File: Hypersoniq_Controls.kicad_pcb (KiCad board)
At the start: 2 copper layers, 40.4 x 110 mm, 15 parts, among them J1 Conn_01x10_Pin, J11 Freq_In, J12 Audio_Mix_4Pole, J2 Conn_01x10_Pin, J3 Conn_01x10_Pin, J4 Audio_In, J5 Audio_Out_1P, J6 Audio_Mix_1Pole, J7 Freq_CV, J8 Audio_Out_4P

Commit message: Started laying out Panel
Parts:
- moved J12 3.20 mm to (83.1, 141.5)
- moved J6 3.20 mm to (57.8, 141.5)
- moved J11 2.10 mm to (70.2, 140.0)
- moved TP4 0.43 mm to (86.9, 147.4)
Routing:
- net /AUDIO_MIX_4POLE: track 66.3 -> 69.5 mm
- net /AUDIO_MIX_1POLE: track 67.0 -> 70.1 mm
- net /FREQ_CV3: track 56.6 -> 58.7 mm
- net /AUDIO_IN3: track 55.1 -> 56.4 mm
- net /AUDIO_IN4: track 57.9 -> 58.9 mm
- net /FREQ_JACK: track 13.7 -> 12.7 mm

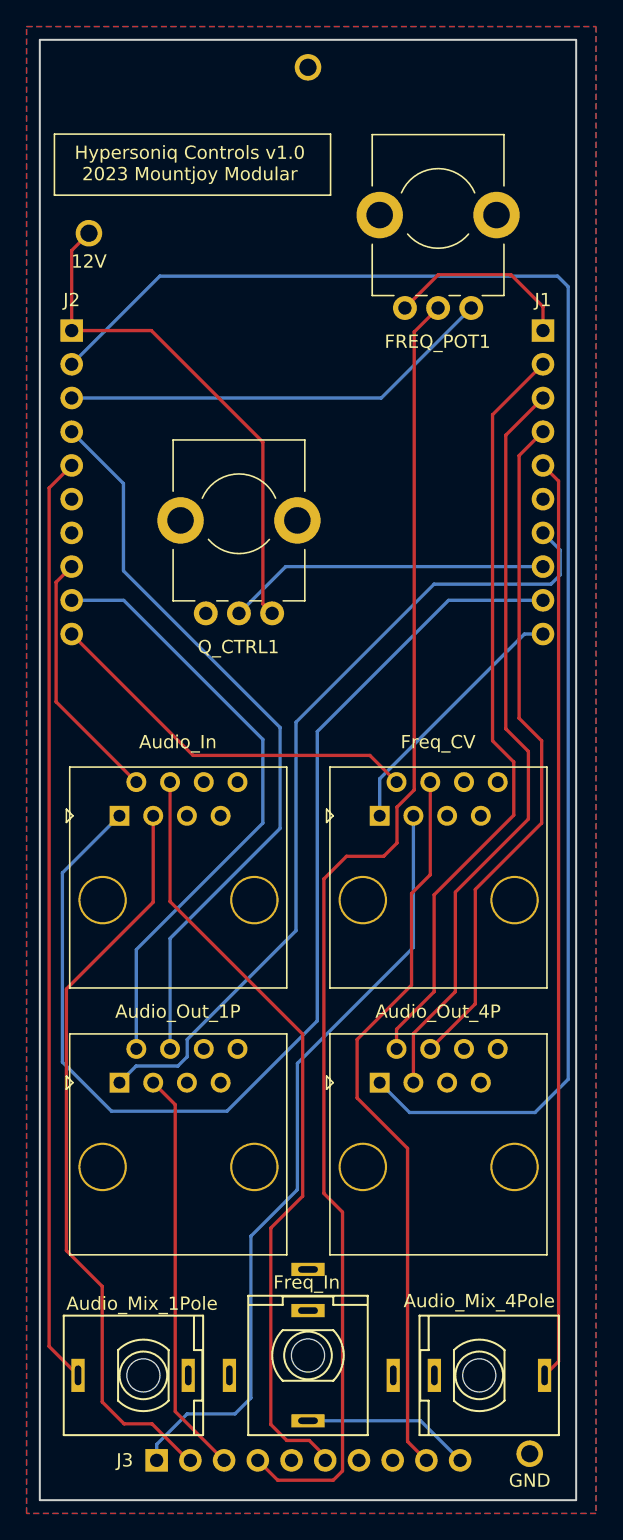
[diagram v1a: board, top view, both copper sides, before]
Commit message: Started generating JLC placement details
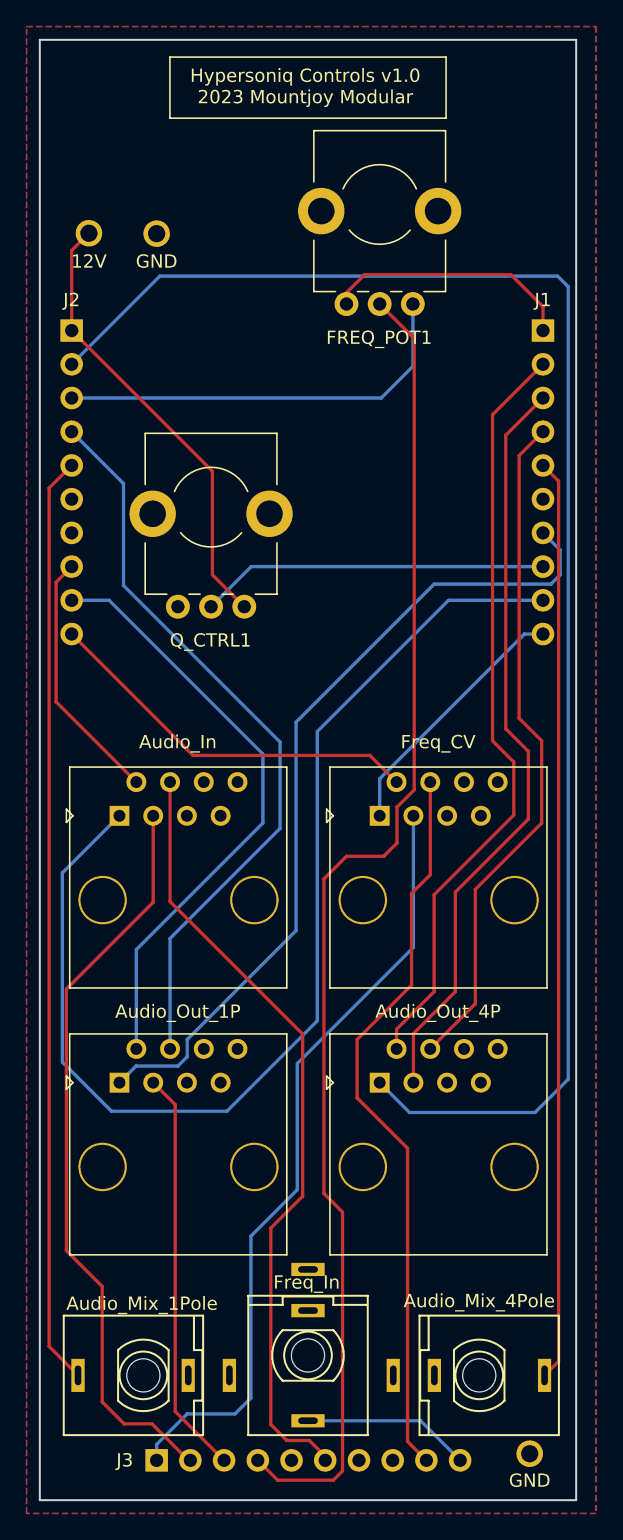
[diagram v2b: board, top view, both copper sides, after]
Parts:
- moved TP3 16.9 mm to (58.8, 55.5)
- moved FREQ_POT1 4.41 mm to (75.6, 53.3)
- moved Q_CTRL1 2.16 mm to (62.9, 76.1)
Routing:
- net +12V: track 38.9 -> 34.1 mm
- net /FREQ_POT_VL: track 14.2 -> 19.0 mm
- net /Q_POT: track 24.4 -> 26.3 mm
- net /FREQ_POT_VH: track 32.9 -> 31.4 mm
- net /1POLE_OUT2: track 46.0 -> 45.4 mm
- net /FREQ_POT: track 100.7 -> 101.3 mm
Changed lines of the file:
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@@
   (net 43 "unconnected-(J12-Pad2)")
   (footprint "Custom_Footprints:1.3mm_Test_Point" (layer "F.Cu")
-    (at 70.2 42.97)
+    (at 58.8 55.5)
     (descr "1.3mm Test Point")
     (tags "Through Hole Mount Test Points")
@@
   )
   (footprint "Custom_Footprints:Alpha_9mm_Potentiometer_Aligned" (layer "F.Cu")
-    (at 65 76.6)
+    (at 62.9 76.1)
     (descr "Potentiometer 9mm")
     (tags "Potentiometer 9mm")
@@
   )
   (footprint "Custom_Footprints:Alpha_9mm_Potentiometer_Aligned" (layer "F.Cu")
-    (at 80 53.6)
+    (at 75.6 53.3)
     (descr "Potentiometer 9mm")
     (tags "Potentiometer 9mm")
@@
     )
   )
-  (gr_rect (start 51.1 48) (end 71.9 52.6)
+  (gr_rect (start 59.8 42.2) (end 80.6 46.8)
     (stroke (width 0.12) (type default)) (fill none) (layer "F.SilkS"))
   (gr_rect (start 57 146.1) (end 83.45 149.7)
@@
   (gr_line (start 90.4 40.9) (end 90.4 150.9)
     (stroke (width 0.15) (type solid)) (layer "Edge.Cuts"))
-  (gr_text "GND" (at 70.2 45) (layer "B.SilkS")
-    (effects (font (size 1.2 1.2) (thickness 0.2)) (justify mirror))
+  (gr_text "GND" (at 58.8 57.53) (layer "B.SilkS")
+    (effects (font (size 1 1) (thickness 0.2)) (justify mirror))
   )
   (gr_text "GND" (at 87 149.43) (layer "B.SilkS")
@@
     (effects (font (size 1 1) (thickness 0.2)) (justify mirror))
   )
+  (gr_text "GND" (at 58.8 57.6) (layer "F.SilkS")
+    (effects (font (size 1 1) (thickness 0.2)))
+  )
   (gr_text "J3" (at 56.4 147.9) (layer "F.SilkS")
     (effects (font (size 1 1) (thickness 0.15)))
   )
-  (gr_text "Hypersoniq Controls v1.0\n2023 Mountjoy Modular" (at 61.3 51.6) (layer "F.SilkS")
+  (gr_text "Hypersoniq Controls v1.0\n2023 Mountjoy Modular" (at 70 45.8) (layer "F.SilkS")
     (effects (font (size 1 1) (thickness 0.15)) (justify bottom))
   )
@@
     (effects (font (size 1 1) (thickness 0.15)))
   )
-  (segment (start 72.8 129.2) (end 72.8 148.7) (width 0.25) (layer "F.Cu") (net 2))
+  (segment (start 76.9 101.4) (end 75.9 102.4) (width 0.25) (layer "F.Cu") (net 2))
+  (segment (start 75.6 60.8) (end 78.2 63.4) (width 0.25) (layer "F.Cu") (net 2))
+  (segment (start 78.2 97.4) (end 76.9 98.7) (width 0.25) (layer "F.Cu") (net 2))
   (segment (start 71.4 104.1) (end 71.4 127.8) (width 0.25) (layer "F.Cu") (net 2))
   (segment (start 75.9 102.4) (end 73.1 102.4) (width 0.25) (layer "F.Cu") (net 2))
-  (segment (start 76.9 101.4) (end 75.9 102.4) (width 0.25) (layer "F.Cu") (net 2))
-  (segment (start 78.2 97.4) (end 76.9 98.7) (width 0.25) (layer "F.Cu") (net 2))
   (segment (start 72.8 148.7) (end 72.1 149.4) (width 0.25) (layer "F.Cu") (net 2))
+  (segment (start 76.9 98.7) (end 76.9 101.4) (width 0.25) (layer "F.Cu") (net 2))
   (segment (start 67.92 149.4) (end 66.42 147.9) (width 0.25) (layer "F.Cu") (net 2))
-  (segment (start 80 61.1) (end 78.2 62.9) (width 0.25) (layer "F.Cu") (net 2))
-  (segment (start 78.2 62.9) (end 78.2 97.4) (width 0.25) (layer "F.Cu") (net 2))
+  (segment (start 78.2 63.4) (end 78.2 97.4) (width 0.25) (layer "F.Cu") (net 2))
+  (segment (start 72.1 149.4) (end 67.92 149.4) (width 0.25) (layer "F.Cu") (net 2))
   (segment (start 73.1 102.4) (end 71.4 104.1) (width 0.25) (layer "F.Cu") (net 2))
-  (segment (start 76.9 98.7) (end 76.9 101.4) (width 0.25) (layer "F.Cu") (net 2))
-  (segment (start 72.1 149.4) (end 67.92 149.4) (width 0.25) (layer "F.Cu") (net 2))
+  (segment (start 72.8 129.2) (end 72.8 148.7) (width 0.25) (layer "F.Cu") (net 2))
   (segment (start 71.4 127.8) (end 72.8 129.2) (width 0.25) (layer "F.Cu") (net 2))
   (segment (start 52.4 67.88) (end 75.72 67.88) (width 0.25) (layer "B.Cu") (net 3))
-  (segment (start 75.72 67.88) (end 82.5 61.1) (width 0.25) (layer "B.Cu") (net 3))
+  (segment (start 75.72 67.88) (end 78.1 65.5) (width 0.25) (layer "B.Cu") (net 3))
+  (segment (start 78.1 65.5) (end 78.1 60.8) (width 0.25) (layer "B.Cu") (net 3))
+  (segment (start 74.45 58.6) (end 73.1 59.95) (width 0.25) (layer "F.Cu") (net 4))
   (segment (start 87.9 62.8) (end 87.9 61) (width 0.25) (layer "F.Cu") (net 4))
-  (segment (start 85.5 58.6) (end 80 58.6) (width 0.25) (layer "F.Cu") (net 4))
+  (segment (start 85.5 58.6) (end 74.45 58.6) (width 0.25) (layer "F.Cu") (net 4))
+  (segment (start 73.1 59.95) (end 73.1 60.8) (width 0.25) (layer "F.Cu") (net 4))
   (segment (start 87.9 61) (end 85.5 58.6) (width 0.25) (layer "F.Cu") (net 4))
-  (segment (start 80 58.6) (end 77.5 61.1) (width 0.25) (layer "F.Cu") (net 4))
   (segment (start 85.7 99.3) (end 85.7 95.3) (width 0.25) (layer "F.Cu") (net 5))
   (segment (start 85.7 95.3) (end 84.1 93.7) (width 0.25) (layer "F.Cu") (net 5))
@@
   (segment (start 51.225 90.765) (end 51.225 81.755) (width 0.25) (layer "F.Cu") (net 14))
   (segment (start 57.27 96.81) (end 51.225 90.765) (width 0.25) (layer "F.Cu") (net 14))
+  (segment (start 56.3 82) (end 68.1 93.8) (width 0.25) (layer "B.Cu") (net 15))
+  (segment (start 59.81 108.59) (end 59.81 116.91) (width 0.25) (layer "B.Cu") (net 15))
+  (segment (start 68.1 93.8) (end 68.1 100.3) (width 0.25) (layer "B.Cu") (net 15))
   (segment (start 52.4 70.42) (end 56.3 74.32) (width 0.25) (layer "B.Cu") (net 15))
-  (segment (start 68.1 92.7) (end 68.1 100.3) (width 0.25) (layer "B.Cu") (net 15))
-  (segment (start 56.3 74.32) (end 56.3 80.9) (width 0.25) (layer "B.Cu") (net 15))
-  (segment (start 59.81 108.59) (end 59.81 116.91) (width 0.25) (layer "B.Cu") (net 15))
+  (segment (start 56.3 74.32) (end 56.3 82) (width 0.25) (layer "B.Cu") (net 15))
   (segment (start 68.1 100.3) (end 59.81 108.59) (width 0.25) (layer "B.Cu") (net 15))
-  (segment (start 56.3 80.9) (end 68.1 92.7) (width 0.25) (layer "B.Cu") (net 15))
   (segment (start 52.88 141.5) (end 50.7 139.32) (width 0.25) (layer "F.Cu") (net 16))
   (segment (start 50.7 139.32) (end 50.7 74.66) (width 0.25) (layer "F.Cu") (net 16))
   (segment (start 50.7 74.66) (end 52.4 72.96) (width 0.25) (layer "F.Cu") (net 16))
-  (segment (start 68.52 80.58) (end 87.9 80.58) (width 0.25) (layer "B.Cu") (net 17))
-  (segment (start 65 84.1) (end 68.52 80.58) (width 0.25) (layer "B.Cu") (net 17))
+  (segment (start 62.9 83.6) (end 65.92 80.58) (width 0.25) (layer "B.Cu") (net 17))
+  (segment (start 65.92 80.58) (end 87.9 80.58) (width 0.25) (layer "B.Cu") (net 17))
   (segment (start 67.4 145.2) (end 67.4 130.4) (width 0.25) (layer "F.Cu") (net 18))
   (segment (start 70.3 146.4) (end 68.6 146.4) (width 0.25) (layer "F.Cu") (net 18))
@@
   (segment (start 67.4 130.4) (end 69.8 128) (width 0.25) (layer "F.Cu") (net 18))
   (segment (start 59.81 105.81) (end 59.81 96.81) (width 0.25) (layer "F.Cu") (net 18))
-  (segment (start 52.4 83.12) (end 56.32 83.12) (width 0.25) (layer "B.Cu") (net 19))
-  (segment (start 66.8 93.6) (end 66.8 99.9) (width 0.25) (layer "B.Cu") (net 19))
+  (segment (start 55.22 83.12) (end 66.8 94.7) (width 0.25) (layer "B.Cu") (net 19))
   (segment (start 57.27 109.43) (end 57.27 116.91) (width 0.25) (layer "B.Cu") (net 19))
   (segment (start 66.8 99.9) (end 57.27 109.43) (width 0.25) (layer "B.Cu") (net 19))
-  (segment (start 56.32 83.12) (end 66.8 93.6) (width 0.25) (layer "B.Cu") (net 19))
+  (segment (start 52.4 83.12) (end 55.22 83.12) (width 0.25) (layer "B.Cu") (net 19))
+  (segment (start 66.8 94.7) (end 66.8 99.9) (width 0.25) (layer "B.Cu") (net 19))
   (segment (start 74.86 94.8) (end 61.54 94.8) (width 0.25) (layer "F.Cu") (net 20))
   (segment (start 76.87 96.81) (end 74.86 94.8) (width 0.25) (layer "F.Cu") (net 20))
@@
   (segment (start 58.8 146.7) (end 61.1 144.4) (width 0.25) (layer "B.Cu") (net 22))
   (segment (start 52.4 56.77) (end 53.7 55.47) (width 0.25) (layer "F.Cu") (net 40))
-  (segment (start 66.8 71.2) (end 58.4 62.8) (width 0.25) (layer "F.Cu") (net 40))
-  (segment (start 58.4 62.8) (end 52.4 62.8) (width 0.25) (layer "F.Cu") (net 40))
-  (segment (start 67.5 84.1) (end 66.8 83.4) (width 0.25) (layer "F.Cu") (net 40))
-  (segment (start 66.8 83.4) (end 66.8 71.2) (width 0.25) (layer "F.Cu") (net 40))
+  (segment (start 63 73.4) (end 52.4 62.8) (width 0.25) (layer "F.Cu") (net 40))
   (segment (start 52.4 62.8) (end 52.4 56.77) (width 0.25) (layer "F.Cu") (net 40))
+  (segment (start 65.4 83.6) (end 63 81.2) (width 0.25) (layer "F.Cu") (net 40))
+  (segment (start 63 81.2) (end 63 73.4) (width 0.25) (layer "F.Cu") (net 40))
   (segment (start 58.54 119.45) (end 60.2 121.11) (width 0.25) (layer "F.Cu") (net 41))
   (segment (start 60.2 144.22) (end 63.88 147.9) (width 0.25) (layer "F.Cu") (net 41))

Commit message: Minor cleanup
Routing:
- net /FREQ_CV1: track 19.6 -> 22.8 mm
- net /AUDIO_IN1: track 86.8 -> 87.4 mm
- net GND: vias 0 -> 24

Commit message: Panel and Control tidy up
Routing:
- net GND: vias 24 -> 34
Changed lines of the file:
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@@
   (via (at 82.9 62.9) (size 0.8) (drill 0.4) (layers "F.Cu" "B.Cu") (free) (net 1))
   (via (at 81.3 89.8) (size 0.8) (drill 0.4) (layers "F.Cu" "B.Cu") (free) (net 1))
+  (via (at 55.9 102.2) (size 0.8) (drill 0.4) (layers "F.Cu" "B.Cu") (free) (net 1))
   (via (at 51.8 148.4) (size 0.8) (drill 0.4) (layers "F.Cu" "B.Cu") (free) (net 1))
   (via (at 66.8 121.9) (size 0.8) (drill 0.4) (layers "F.Cu" "B.Cu") (free) (net 1))
   (via (at 58 64) (size 0.8) (drill 0.4) (layers "F.Cu" "B.Cu") (free) (net 1))
+  (via (at 62.2 111.1) (size 0.8) (drill 0.4) (layers "F.Cu" "B.Cu") (free) (net 1))
   (via (at 67.7 116.5) (size 0.8) (drill 0.4) (layers "F.Cu" "B.Cu") (free) (net 1))
   (via (at 87 133.9) (size 0.8) (drill 0.4) (layers "F.Cu" "B.Cu") (free) (net 1))
   (via (at 88 88.5) (size 0.8) (drill 0.4) (layers "F.Cu" "B.Cu") (free) (net 1))
   (via (at 73 113.1) (size 0.8) (drill 0.4) (layers "F.Cu" "B.Cu") (free) (net 1))
+  (via (at 76.6 103.6) (size 0.8) (drill 0.4) (layers "F.Cu" "B.Cu") (free) (net 1))
+  (via (at 84.6 109.5) (size 0.8) (drill 0.4) (layers "F.Cu" "B.Cu") (free) (net 1))
+  (via (at 73.2 122.6) (size 0.8) (drill 0.4) (layers "F.Cu" "B.Cu") (free) (net 1))
   (via (at 56.4 129.9) (size 0.8) (drill 0.4) (layers "F.Cu" "B.Cu") (free) (net 1))
   (via (at 62 92) (size 0.8) (drill 0.4) (layers "F.Cu" "B.Cu") (free) (net 1))
   (via (at 81.7 124.7) (size 0.8) (drill 0.4) (layers "F.Cu" "B.Cu") (free) (net 1))
   (via (at 87.9 55.3) (size 0.8) (drill 0.4) (layers "F.Cu" "B.Cu") (free) (net 1))
+  (via (at 68.2 90.7) (size 0.8) (drill 0.4) (layers "F.Cu" "B.Cu") (free) (net 1))
   (via (at 81 77.8) (size 0.8) (drill 0.4) (layers "F.Cu" "B.Cu") (free) (net 1))
+  (via (at 66.3 109) (size 0.8) (drill 0.4) (layers "F.Cu" "B.Cu") (free) (net 1))
   (via (at 64 70.1) (size 0.8) (drill 0.4) (layers "F.Cu" "B.Cu") (free) (net 1))
   (via (at 56.2 70.3) (size 0.8) (drill 0.4) (layers "F.Cu" "B.Cu") (free) (net 1))
+  (via (at 75.5 130) (size 0.8) (drill 0.4) (layers "F.Cu" "B.Cu") (free) (net 1))
   (via (at 54.3 90.2) (size 0.8) (drill 0.4) (layers "F.Cu" "B.Cu") (free) (net 1))
   (via (at 63.2 131.2) (size 0.8) (drill 0.4) (layers "F.Cu" "B.Cu") (free) (net 1))
   (via (at 55.6 85.6) (size 0.8) (drill 0.4) (layers "F.Cu" "B.Cu") (free) (net 1))
   (via (at 75.8 82) (size 0.8) (drill 0.4) (layers "F.Cu" "B.Cu") (free) (net 1))
+  (via (at 53.8 122.8) (size 0.8) (drill 0.4) (layers "F.Cu" "B.Cu") (free) (net 1))
+  (via (at 68.2 102.9) (size 0.8) (drill 0.4) (layers "F.Cu" "B.Cu") (free) (net 1))
   (via (at 53.9 117.1) (size 0.8) (drill 0.4) (layers "F.Cu" "B.Cu") (free) (net 1))
   (via (at 87.2 118.1) (size 0.8) (drill 0.4) (layers "F.Cu" "B.Cu") (free) (net 1))

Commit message: v1.0 Design sent for manufacture
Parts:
- J1, J2, J3: footprint Connector_PinHeader_2.54mm:PinHeader_1x10_P2.54mm_Vertical -> Connector_PinSocket_2.54mm:PinSocket_1x10_P2.54mm_Vertical
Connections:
- J3 pad 5: GND -> -12V
